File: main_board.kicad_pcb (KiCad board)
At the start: 2 copper layers, 113.5 x 55.1 mm, 49 parts, among them J104 HEADER_2, J105 HEADER_4, J106 HEADER_2, J107 HEADER_4x2, J108 HEADER_6, M101 MOUNTING-HOLE, M102 MOUNTING-HOLE, M103 MOUNTING-HOLE, M104 MOUNTING-HOLE, M105 MOUNTING-HOLE, SW101 SPST, SW102 SPST, SW103 SPST, SW104 SPST, SW105 SPST, SW106 SPST, SW107 SPST, SW108 SPST, SW109 SPST, SW110 SPST, SW111 SPST, SW112 SPST, SW113 SPST, SW114 SPST, SW115 SPST, SW116 SPST, SW117 SPST, SW118 SPST, SW119 SPST, SW120 SPST, SW121 SPST, SW122 SPST, SW123 SPST, SW124 SPST, SW125 SPST, SW126 SPST, SW127 SPST, SW128 SPST, U101 Teensy-LC, U102 ESP-12E

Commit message: Final main board v0.1
Last big upload commit before I start doing proper commits ;)
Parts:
- removed J107: HEADER_4x2, Socket_Strips:Socket_Strip_Straight_2x04
- added J1: HEADER_5x2, Socket_Strips:Socket_Strip_Straight_2x05, B.Cu at (101.0, 81.9)
- added J2: HEADER_1, Socket_Strips:Socket_Strip_Straight_1x01, F.Cu at (107.3, 92.1)
- added U1: ESP-01v090, ESP8266:ESP-01, B.Cu at (189.2, 90.2)
- J106: footprint Socket_Strips:Socket_Strip_Straight_1x02 -> w_conn_jst-ph:b2b-ph-kl
- J108: footprint Socket_Strips:Socket_Strip_Straight_1x06 -> Pin_Headers:Pin_Header_Angled_1x06
- R101, R102: moved to F.Cu
- moved J108 12.8 mm to (124.5, 67.9), turned to 90 degrees
- moved R107 7.73 mm to (111.8, 74.9), turned to 90 degrees
- moved R106 5.68 mm to (115.6, 89.5), turned to 90 degrees
- moved J106 5.24 mm to (120.7, 90.2)
- moved U101 5.08 mm to (157.5, 95.2)
- moved J104 3.81 mm to (119.4, 95.2)
- moved R101 2.62 mm to (196.8, 98.4), turned to 270 degrees
- moved R102 2.54 mm to (192.4, 98.4), turned to 270 degrees
- moved J105 2.54 mm to (124.5, 85.1)
- moved D101 2.51 mm to (111.4, 79.0), turned to 225 degrees
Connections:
- J108 pad 2: Net-(J108-Pad2) -> /TEENSY_TX
- J108 pad 3: +BATT -> /ESP_RX
- J108 pad 4: /FTDI_TX -> /TEENSY_RX
- J108 pad 5: /FTDI_RX -> /ESP_TX
- J108 pad 6: Net-(J108-Pad6) -> +BATT
- U101 pad 11: /KM_COL5 -> Net-(U101-Pad11)
- U101 pad 12: /KM_COL6 -> /BUZZER
- U101 pad 13: Net-(U101-Pad13) -> /KM_COL5
- U101 pad 14: Net-(U101-Pad14) -> /KM_COL6
- U101 pad 2: /ESP_TX -> /TEENSY_RX
- U101 pad 3: /ESP_RX -> /TEENSY_TX
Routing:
- net /BUZZER: track 0.00 -> 77.3 mm, vias 0 -> 5
- net /TEENSY_RX: track 0.00 -> 42.4 mm
- net /ESP_TX: track 69.0 -> 109.7 mm, vias 5 -> 1
- net /TEENSY_TX: track 0.00 -> 39.4 mm
- net /ESP_RX: track 63.5 -> 100.0 mm, vias 5 -> 0
- net +3.3V: track 138.1 -> 156.2 mm, vias 3 -> 4
- net /KM_COL6: track 106.7 -> 89.4 mm
- net /KM_COL5: track 127.4 -> 113.2 mm
- net Net-(R104-Pad2): track 3.82 -> 17.7 mm
- net Net-(R103-Pad2): track 3.38 -> 17.1 mm
- net /KM_COL2: track 81.8 -> 91.9 mm
- net /KM_COL3: track 103.0 -> 112.6 mm
- net Net-(R101-Pad2): track 2.77 -> 12.2 mm, vias 0 -> 2
- net Net-(R102-Pad2): track 2.77 -> 12.0 mm, vias 0 -> 2
- net /STATUS_LED: track 41.8 -> 48.0 mm
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- removed copper zone on B.Cu, net GND
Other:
- net class Power: trace_width 0.381 -> 0.508
- board text added: "ESP-01"
- board text added: "ESP-12E"
- board text added: "It's so bad."
- board text added: "Power Glove UHID Main Board v0.1"

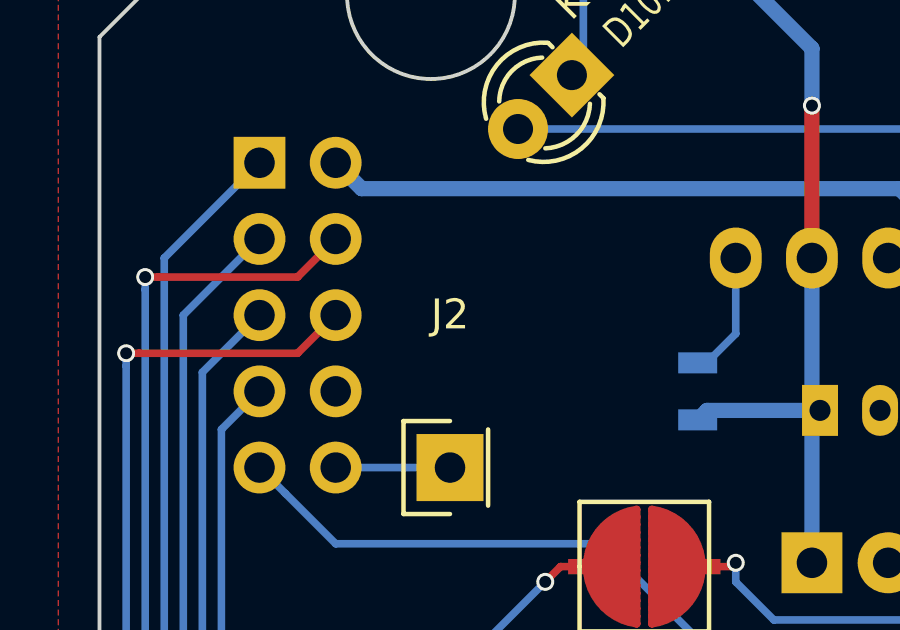
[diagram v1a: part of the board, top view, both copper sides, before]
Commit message: Rearranged sensor board components for cleanliness
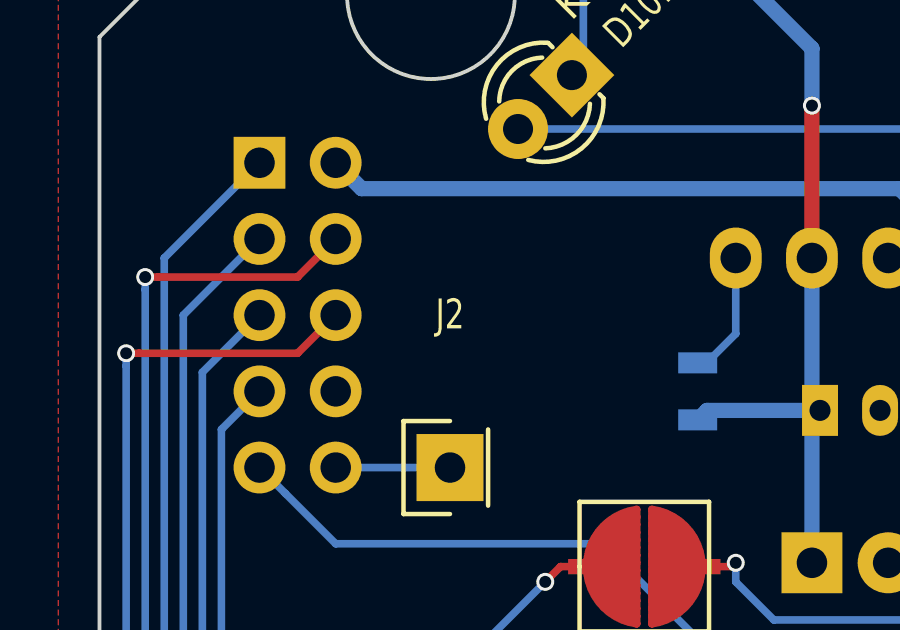
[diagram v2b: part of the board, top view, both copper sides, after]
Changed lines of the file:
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@@
     (links 107)
     (no_connects 1)
-    (area 95.567499 63.817499 209.232501 119.062501)
+    (area 86.894999 57.015999 217.905001 120.370601)
     (thickness 1.6)
     (drawings 45)
@@
     (nets 60)
   )
-  (page A4)
+  (page USLetter)
+  (title_block
+    (title "Power Glove UHID Main Board")
+    (date 2016-03-24)
+    (rev 0.1)
+  )
   (layers
     (0 Top signal)
@@
     (tags "Module ESP-8266 ESP8266")
     (fp_text reference U1 (at 0.254 4.572 270) (layer B.SilkS)
-      (effects (font (size 1 1) (thickness 0.15)) (justify mirror))
+      (effects (font (size 1 0.75) (thickness 0.15)) (justify mirror))
     )
     (fp_text value ESP-01v090 (at 12.192 -3.556 270) (layer B.Fab)
@@
     (tags "socket strip")
     (fp_text reference J1 (at -2.54 -1.27 360) (layer B.SilkS)
-      (effects (font (size 1 1) (thickness 0.15)) (justify mirror))
+      (effects (font (size 1 0.75) (thickness 0.15)) (justify mirror))
     )
     (fp_text value HEADER_5x2 (at 0 3.1 270) (layer B.Fab)
@@
     (tags "socket strip")
     (fp_text reference J2 (at 0 -5.1) (layer F.SilkS)
-      (effects (font (size 1 1) (thickness 0.15)))
+      (effects (font (size 1 0.75) (thickness 0.15)))
     )
     (fp_text value HEADER_1 (at 0 -3.1) (layer F.Fab)
@@
   (segment (start 129.794 67.056) (end 130.175 66.675) (width 0.254) (layer Top) (net 12))
   (via (at 130.175 66.675) (size 0.6) (drill 0.4) (layers Top Bottom) (net 12))
-  (via (at 133.985 85.09) (size 0.6) (drill 0.4) (layers Top Bottom) (net 13) (status 1000000))
+  (via (at 133.985 85.09) (size 0.6) (drill 0.4) (layers Top Bottom) (net 13))
   (segment (start 133.985 85.09) (end 133.985 89.535) (width 0.254) (layer Top) (net 13))
   (segment (start 154.305 89.535) (end 133.985 89.535) (width 0.254) (layer Bottom) (net 13))

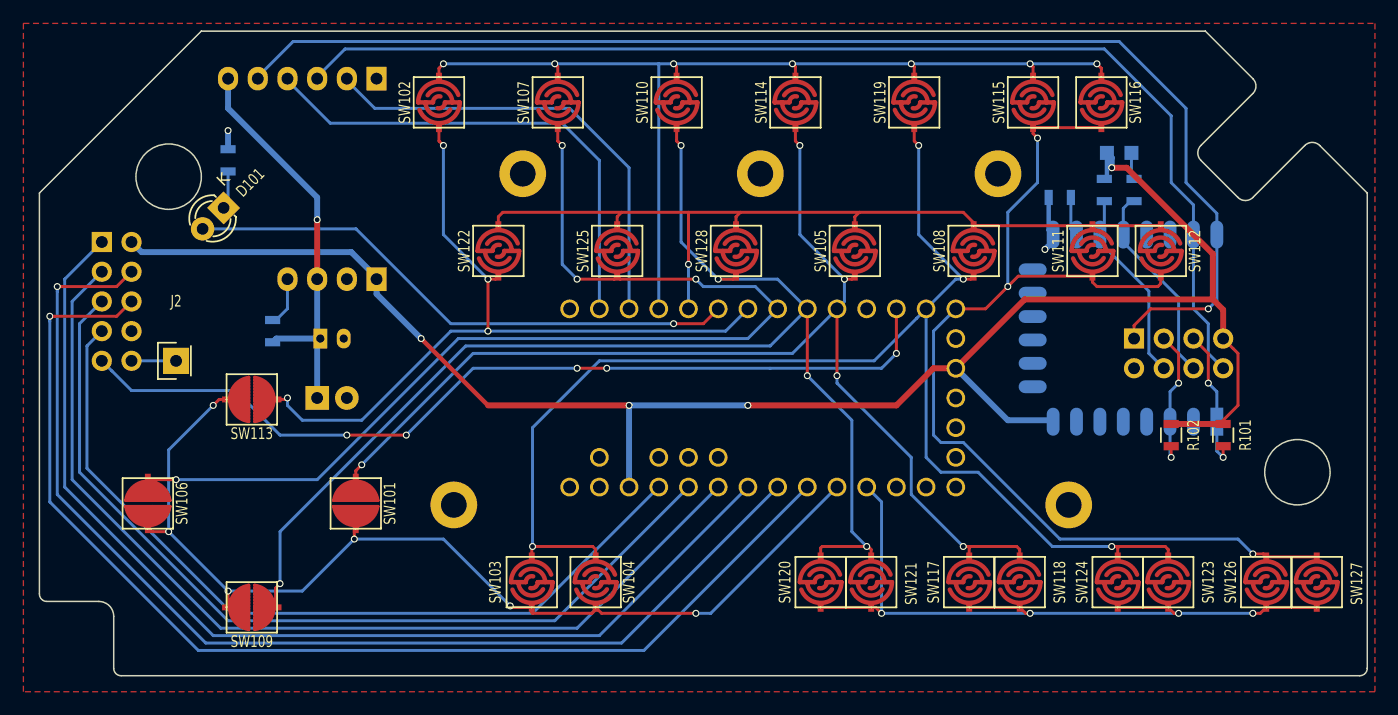
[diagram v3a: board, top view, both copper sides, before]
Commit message: Bumped version to 0.2, cleaned schematic, added voltage divider resistors, boot and reset buttons
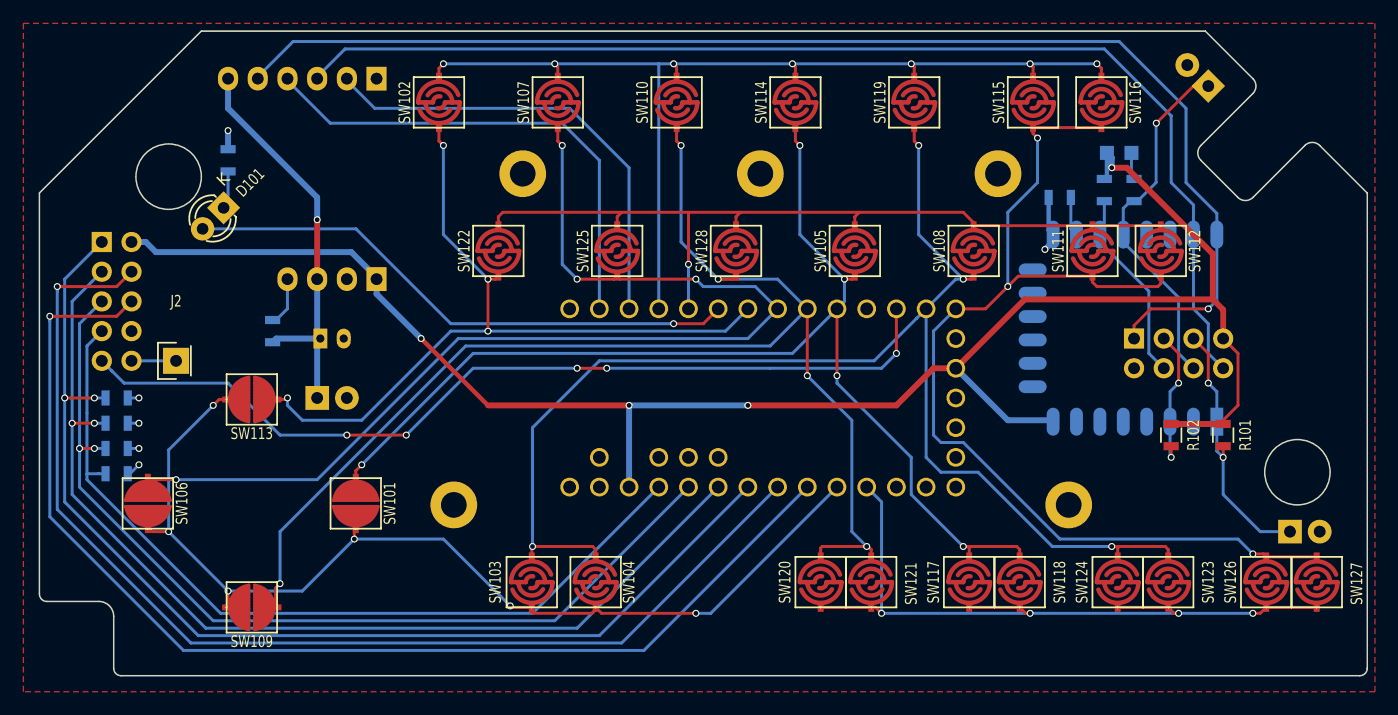
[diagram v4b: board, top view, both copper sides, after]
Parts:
- added R108: 22k, Resistors_SMD:R_0805, B.Cu at (102.2, 95.2)
- added R109: 22k, Resistors_SMD:R_0805, B.Cu at (102.2, 97.4)
- added R110: 22k, Resistors_SMD:R_0805, B.Cu at (102.2, 99.6)
- added R111: 22k, Resistors_SMD:R_0805, B.Cu at (102.2, 101.7)
- added SW129: SPST, Socket_Strips:Socket_Strip_Straight_1x02, B.Cu at (195.6, 68.6)
- added SW130: SPST, Socket_Strips:Socket_Strip_Straight_1x02, B.Cu at (202.6, 106.7)
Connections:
- net Net-(R101-Pad2) renamed /ESP_RESET
- net Net-(R102-Pad2) renamed /ESP_EN
- net Net-(R103-Pad2) renamed /ESP_GPIO2
- net Net-(R104-Pad2) renamed /ESP_GPIO0
- net Net-(R105-Pad1) renamed /ESP_GPIO15
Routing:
- net /ESP_GPIO0: track 17.7 -> 31.1 mm, vias 0 -> 1
- net /ESP_RESET: track 12.2 -> 22.4 mm
- net /FLEX1: track 91.2 -> 95.5 mm, vias 0 -> 2
- net GND: track 6.48 -> 10.6 mm, vias 2 -> 6
- net /FLEX2: track 84.3 -> 87.9 mm, vias 0 -> 2
- net /FLEX3: track 77.5 -> 80.4 mm, vias 0 -> 2
- net /FLEX4: track 70.8 -> 72.9 mm
- net /I2C_SDA: track 99.2 -> 99.9 mm
- net /I2C_SCL: track 97.0 -> 97.8 mm
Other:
- board text added: "Power Glove UHID Main Board v0.2"
- board text removed: "Power Glove UHID Main Board v0.1"
